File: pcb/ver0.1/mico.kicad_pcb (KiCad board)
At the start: 2 copper layers, 26.8 x 16 mm, 41 parts, among them J1 USB_A, J2 SWD Prog, U1 MCP1702, U2 MP23DB01HPTR, U3 W25Q128JV, U4 RP2040, U5 logo, Y1 H130B-12.000-20-3050-EXT-TR

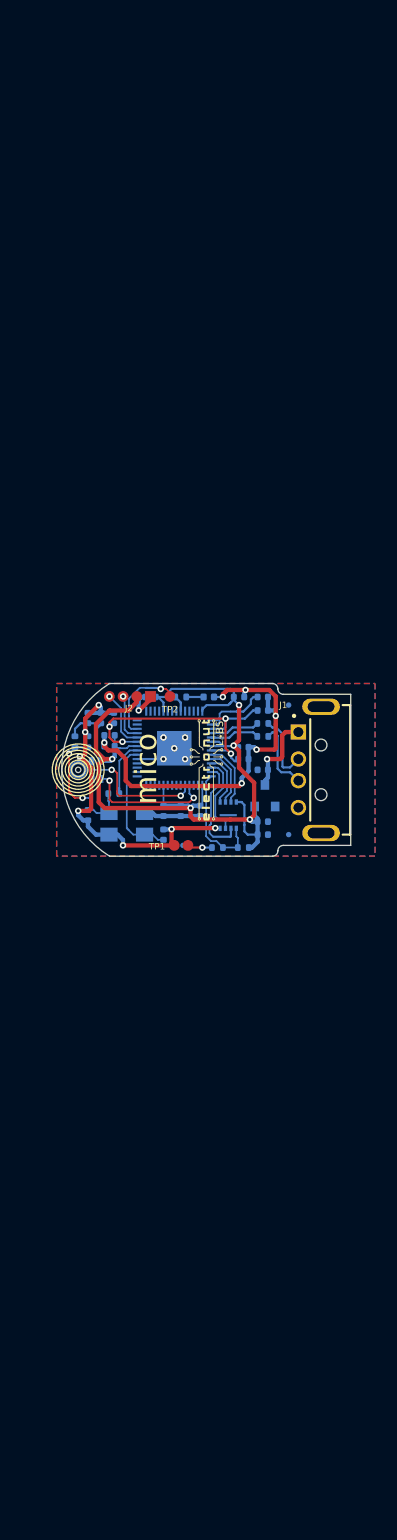
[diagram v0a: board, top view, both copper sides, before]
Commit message: finsh schematic, resize pcb layers and edge cuts for 140mm mic array
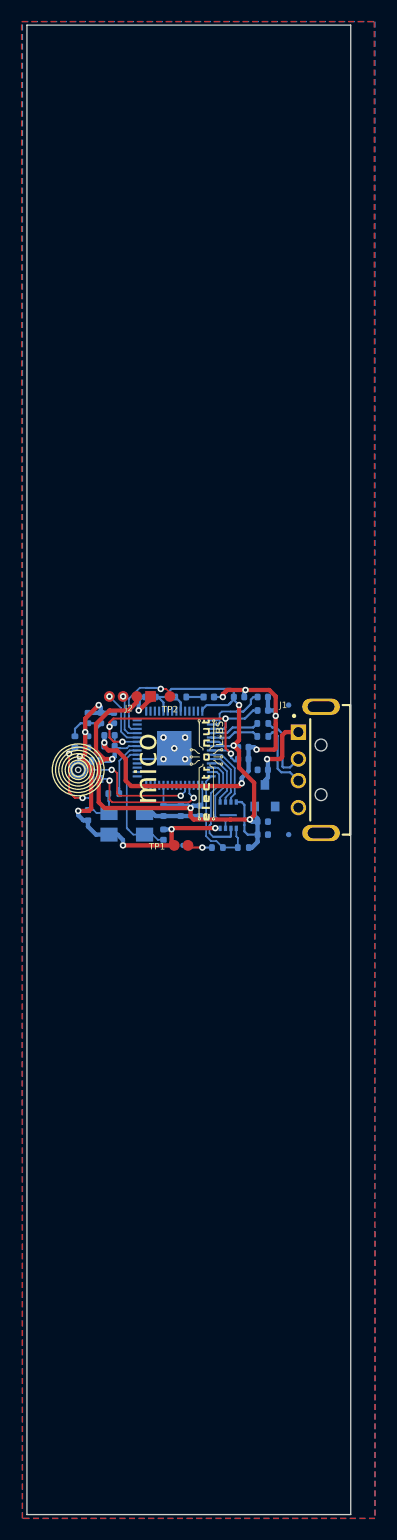
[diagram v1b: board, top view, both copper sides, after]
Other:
- board size 26.8 x 16 mm -> 30 x 138 mm
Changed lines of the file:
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@@
-(kicad_pcb (version 20171130) (host pcbnew "(5.1.12)-1")
+(kicad_pcb (version 20171130) (host pcbnew 5.1.5+dfsg1-2build2)
   (general
     (thickness 2)
-    (drawings 20)
+    (drawings 14)
     (tracks 419)
     (zones 0)
@@
     (0 F.Cu signal)
     (31 B.Cu signal)
-    (32 B.Adhes user)
-    (33 F.Adhes user)
-    (34 B.Paste user)
-    (35 F.Paste user)
-    (36 B.SilkS user)
-    (37 F.SilkS user)
-    (38 B.Mask user)
-    (39 F.Mask user)
+    (32 B.Adhes user hide)
+    (33 F.Adhes user hide)
+    (34 B.Paste user hide)
+    (35 F.Paste user hide)
+    (36 B.SilkS user hide)
+    (37 F.SilkS user hide)
+    (38 B.Mask user hide)
+    (39 F.Mask user hide)
     (40 Dwgs.User user hide)
     (41 Cmts.User user hide)
-    (42 Eco1.User user)
-    (43 Eco2.User user)
+    (42 Eco1.User user hide)
+    (43 Eco2.User user hide)
     (44 Edge.Cuts user)
-    (45 Margin user)
-    (46 B.CrtYd user)
+    (45 Margin user hide)
+    (46 B.CrtYd user hide)
     (47 F.CrtYd user hide)
     (48 B.Fab user hide)
@@
   )
   (setup
-    (last_trace_width 0.2)
+    (last_trace_width 0.16)
     (user_trace_width 0.2)
     (user_trace_width 0.4)
@@
       (xy 1.756833 -1.524) (xy 1.819221 -1.560942) (xy 1.887181 -1.55842)) (layer F.SilkS) (width 0.01))
   )
+  (gr_line (start 146.75 181) (end 116.75 181) (layer Edge.Cuts) (width 0.05))
+  (gr_line (start 116.75 181) (end 116.75 43) (layer Edge.Cuts) (width 0.05))
+  (gr_line (start 146.75 43) (end 116.75 43) (layer Edge.Cuts) (width 0.05))
+  (gr_line (start 146.75 181) (end 146.75 43) (layer Edge.Cuts) (width 0.05))
   (gr_circle (center 121.5 112) (end 123.9 112.1) (layer F.SilkS) (width 0.12))
   (gr_circle (center 121.5 112) (end 123.6 112) (layer F.SilkS) (width 0.12))
@@
   (gr_circle (center 121.5 112) (end 122.7 111.9) (layer F.SilkS) (width 0.12))
   (gr_circle (center 121.5 112) (end 122.4 112) (layer F.SilkS) (width 0.12))
-  (gr_arc (start 139.5 119.5) (end 139.5 120) (angle -90) (layer Edge.Cuts) (width 0.05))
-  (gr_arc (start 140.5 119.5) (end 140.5 119) (angle -90) (layer Edge.Cuts) (width 0.05))
-  (gr_arc (start 139.5 104.5) (end 140 104.5) (angle -90) (layer Edge.Cuts) (width 0.05))
-  (gr_arc (start 140.5 104.5) (end 140 104.5) (angle -90) (layer Edge.Cuts) (width 0.05))
   (gr_text mico (at 127.8 111.9 90) (layer F.SilkS)
     (effects (font (size 2 2) (thickness 0.2)))
@@
   )
   (gr_circle (center 121.5 112) (end 122.132456 112) (layer F.SilkS) (width 0.12))
-  (gr_line (start 146.75 119) (end 146.75 105) (layer Edge.Cuts) (width 0.05))
-  (gr_line (start 140.5 119) (end 146.75 119) (layer Edge.Cuts) (width 0.05))
-  (gr_arc (start 129.4 112) (end 124.4 104) (angle -115.9892336) (layer Edge.Cuts) (width 0.05))
   (gr_text mico (at 145.6 112.1 -90) (layer B.SilkS)
     (effects (font (size 1.5 1.5) (thickness 0.15)) (justify mirror))
   )
-  (gr_line (start 139.5 120) (end 124.4 120) (layer Edge.Cuts) (width 0.05))
-  (gr_line (start 139.5 104) (end 124.4 104) (layer Edge.Cuts) (width 0.05))
-  (gr_line (start 146.75 105) (end 140.5 105) (layer Edge.Cuts) (width 0.05))
   (via (at 139 111) (size 0.6) (drill 0.3) (layers F.Cu B.Cu) (net 1))
   (segment (start 139.08 111.08) (end 139 111) (width 0.4) (layer B.Cu) (net 1))
@@
     (polygon
       (pts
-        (xy 149 104) (xy 149 120) (xy 119.5 120) (xy 119.5 104)
+        (xy 149 42.672) (xy 149 181.356) (xy 116.332 181.356) (xy 116.332 42.672)
       )
     )
@@
     (polygon
       (pts
-        (xy 149 104) (xy 149 120) (xy 119.5 120) (xy 119.5 104)
+        (xy 148.922 42.672) (xy 149 181.356) (xy 116.332 181.356) (xy 116.254 42.672)
       )
     )
